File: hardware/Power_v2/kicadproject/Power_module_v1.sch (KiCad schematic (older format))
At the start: 63 parts, among them J1 Conn_01x02, J2 Conn_02x03_motherboardconn, J3 USB_B_Micro, J4 Conn_01x02_battery, J5 Conn_01x06_programmer, J6 Conn_01x06_programmer, SW1 SW_Push, U1 BQ24040, U2 BQ25570, U3 TPS705, U4 PIC16F18446

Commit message: Power: HW buck layout
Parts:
- added CBATT1, COUT3, CSTOR2: DNP, Capacitor_SMD:C_0805_2012Metric_Pad1.18x1.45mm_HandSolder, symbol Device:C
- added CIN2: 100n, Capacitor_SMD:C_0805_2012Metric_Pad1.18x1.45mm_HandSolder, symbol Device:C
- added COUT2: 22 uF, Capacitor_SMD:C_0805_2012Metric_Pad1.18x1.45mm_HandSolder, symbol Device:C
- C1, C10, C11, C12, C13, C14, C2, C3, C4, C7, C8, C9, CBYP1, CIN1, CREF1, CSTOR1: footprint Capacitor_SMD:C_0805_2012Metric_Pad1.15x1.40mm_HandSolder -> Capacitor_SMD:C_0805_2012Metric_Pad1.18x1.45mm_HandSolder
- COUT1: value 22 uF -> 100n; footprint Capacitor_SMD:C_0805_2012Metric_Pad1.15x1.40mm_HandSolder -> Capacitor_SMD:C_0805_2012Metric_Pad1.18x1.45mm_HandSolder
- J3: symbol Connector:USB_B_Micro -> Power_module_v1-rescue:USB_B_Micro-Connector
- S1, S2, S3: symbol TPS22860:TPS22860 -> Power_module_v1-rescue:TPS22860-TPS22860
- U1: symbol BQ24040:BQ24040 -> Power_module_v1-rescue:BQ24040-BQ24040
- U3: symbol tps7a05:TPS705 -> Power_module_v1-rescue:TPS705-tps7a05
- U4: symbol PIC16F18446SSOP20pin:PIC16F18446 -> Power_module_v1-rescue:PIC16F18446-PIC16F18446SSOP20pin
- renumbered C5 to COUT4, ROK3 to ROK1, ROK1 to ROK3, ROUT2 to ROUT1, ROUT1 to ROUT2, ROV2 to ROV1, ROV1 to ROV2
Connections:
- net 3V3BUCK: now also COUT2.1, COUT3.1
- net BAT+: now also CBATT1.1
- net GND: now also CBATT1.2, CIN2.2, COUT2.2, COUT3.2, CSTOR2.2
- net SOL+: now also CIN2.1
- net VSTOR: now also CSTOR2.1
- net nCHG: now reaches U4.5 (RC5)
- net nCHG: now also D2.1 (K), U1.8 (/CHG)
- no-connect marks 18 -> 17
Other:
- note added: "TODO\nCheck values"
- note added: "X7R\n"
- moved on the sheet: C10, C6, C7, CBYP1, COUT4, CSTOR1, D2, R5, S1

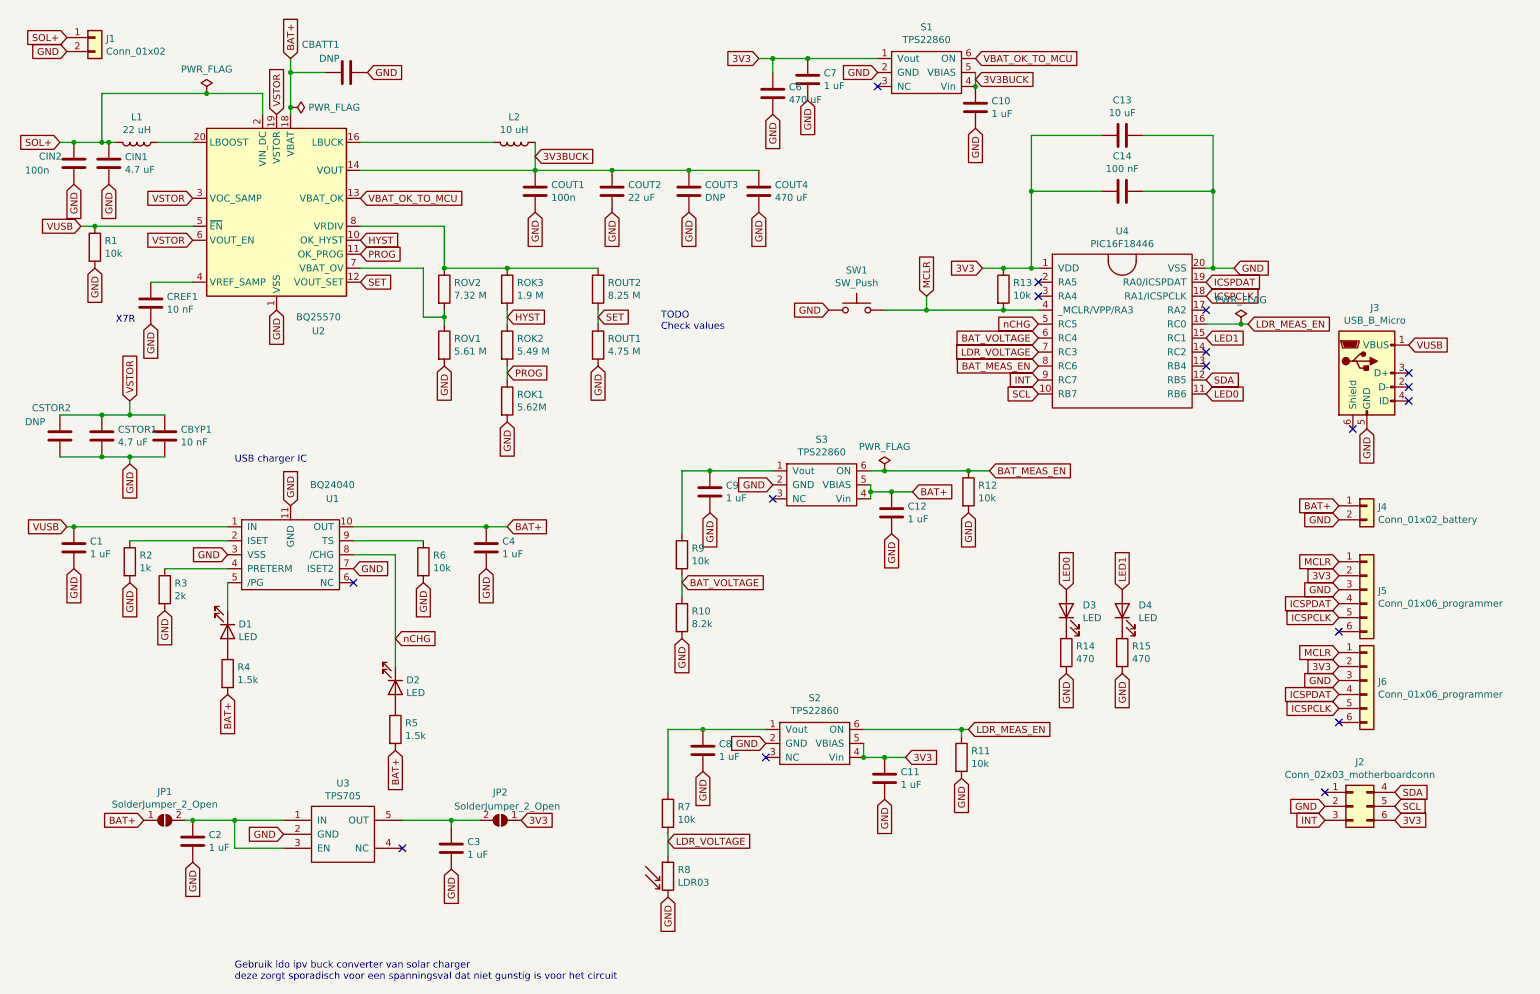
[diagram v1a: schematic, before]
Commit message: Power module HW redesign v2.0
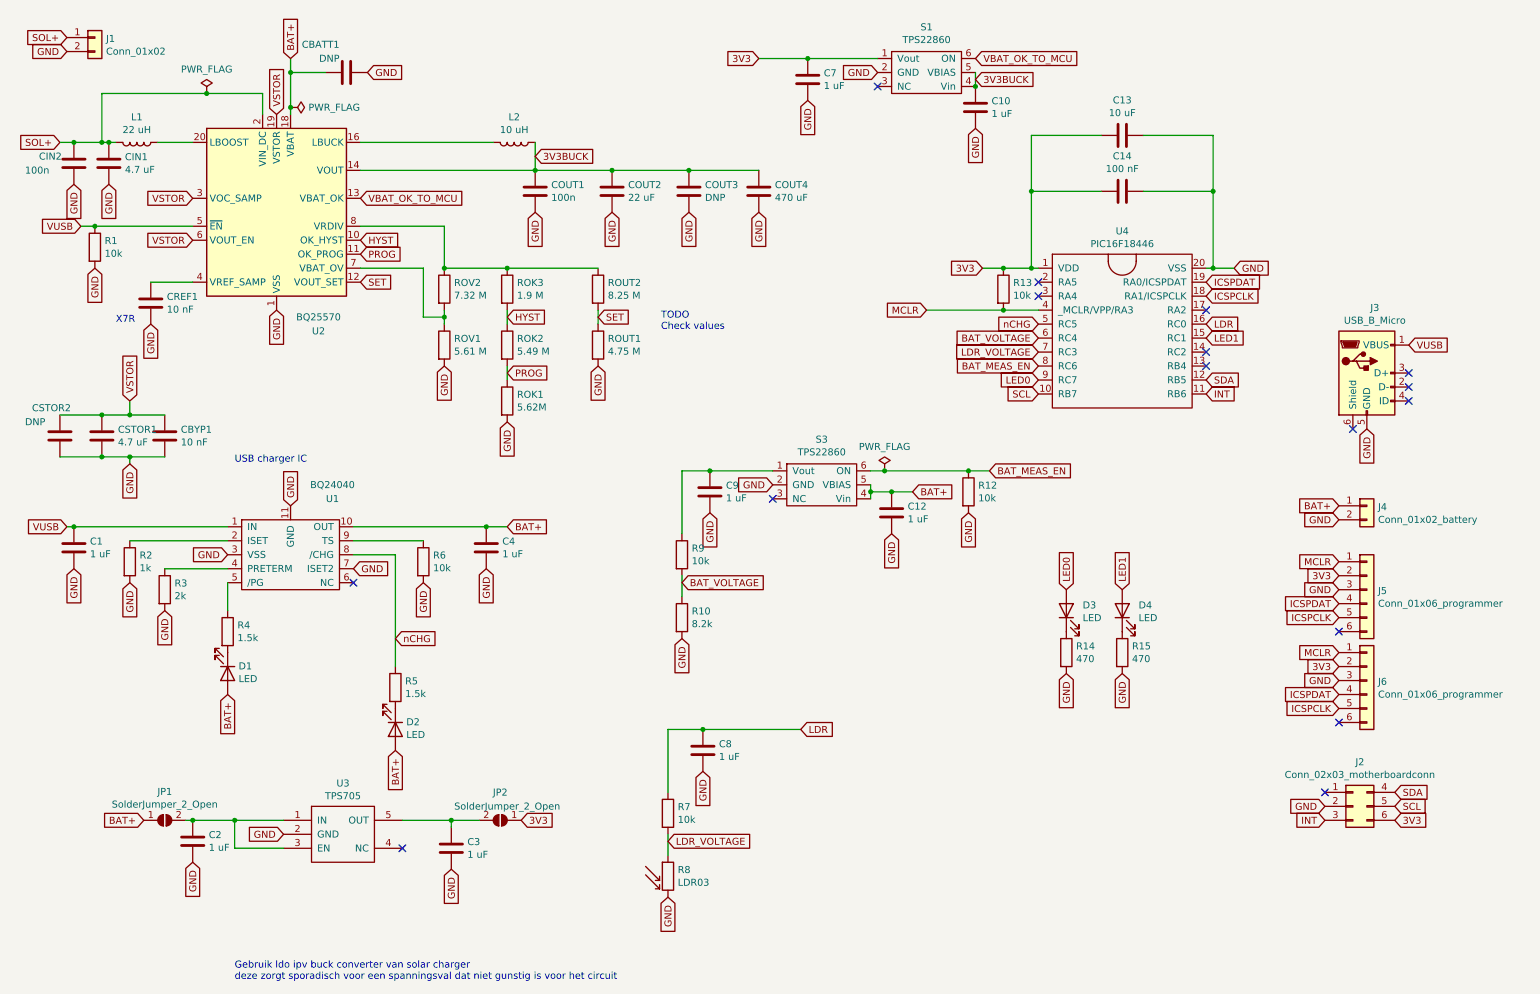
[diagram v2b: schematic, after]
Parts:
- removed C11: 1 uF, Capacitor_SMD:C_0805_2012Metric_Pad1.18x1.45mm_HandSolder, symbol Device:C
- removed C6: 470 uF, Capacitor_THT:CP_Radial_D6.3mm_P2.50mm, symbol Device:C
- removed R11: 10k, Resistor_SMD:R_0805_2012Metric_Pad1.15x1.40mm_HandSolder, symbol Device:R
- removed S2: TPS22860, Package_TO_SOT_SMD:SOT-23-6_Handsoldering, symbol Power_module_v1-rescue:TPS22860-TPS22860
- removed SW1: SW_Push, Button_Switch_THT:SW_PUSH_6mm_H7.3mm, symbol Switch:SW_Push
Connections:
- net LDR_MEAS_EN is gone; now on net LDR: U4.16 (RC0)
- net BAT+: now also D1.2 (A), D2.2 (A); no longer R4.2, R5.2
- net INT: now also U4.11 (RB6); no longer U4.9 (RC7)
- net LED0: now also U4.9 (RC7); no longer U4.11 (RB6)
- net nCHG: now also R5.1; no longer D2.1 (K)
- net at U1.5 (/PG): now also R4.1; no longer D1.1 (K)
- net LDR: now reaches C8.1, R7.1
- new net: D1.1 (K), R4.2
- new net: D2.1 (K), R5.2
- no-connect marks 17 -> 16
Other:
- moved on the sheet: D1, D2
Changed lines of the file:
@@
 L Device:LED D1
 U 1 1 5EE159F7
-P 1950 4900
-F 0 "D1" V 1897 4978 50  0000 L CNN
-F 1 "LED" V 1988 4978 50  0000 L CNN
-F 2 "LED_SMD:LED_0805_2012Metric_Pad1.15x1.40mm_HandSolder" H 1950 4900 50  0001 C CNN
-F 3 "~" H 1950 4900 50  0001 C CNN
-	1    1950 4900
-	0    1    1    0
-$EndComp
-Wire Wire Line
-	1950 4550 1950 4750
-$Comp
-L Device:R R4
-U 1 1 5EE1732A
 P 1950 5200
-F 0 "R4" H 2020 5246 50  0000 L CNN
-F 1 "1.5k" H 2020 5155 50  0000 L CNN
-F 2 "Resistor_SMD:R_0805_2012Metric_Pad1.15x1.40mm_HandSolder" V 1880 5200 50  0001 C CNN
+F 0 "D1" V 1897 5278 50  0000 L CNN
+F 1 "LED" V 1988 5278 50  0000 L CNN
+F 2 "LED_SMD:LED_0805_2012Metric_Pad1.15x1.40mm_HandSolder" H 1950 5200 50  0001 C CNN
 F 3 "~" H 1950 5200 50  0001 C CNN
 	1    1950 5200
-	1    0    0    -1
-$EndComp
+	0    1    1    0
+$EndComp
+Wire Wire Line
+	1950 4550 1950 4750
 Text GLabel 1950 5350 3    50   Input ~ 0
 BAT+
@@
 L Device:LED D2
 U 1 1 5EE1A8AA
-P 3150 5300
-F 0 "D2" V 3097 5378 50  0000 L CNN
-F 1 "LED" V 3188 5378 50  0000 L CNN
-F 2 "LED_SMD:LED_0805_2012Metric_Pad1.15x1.40mm_HandSolder" H 3150 5300 50  0001 C CNN
-F 3 "~" H 3150 5300 50  0001 C CNN
-	1    3150 5300
-	0    1    1    0
-$EndComp
-$Comp
-L Device:R R5
-U 1 1 5EE1A8B0
 P 3150 5600
-F 0 "R5" H 3220 5646 50  0000 L CNN
-F 1 "1.5k" H 3220 5555 50  0000 L CNN
-F 2 "Resistor_SMD:R_0805_2012Metric_Pad1.15x1.40mm_HandSolder" V 3080 5600 50  0001 C CNN
+F 0 "D2" V 3097 5678 50  0000 L CNN
+F 1 "LED" V 3188 5678 50  0000 L CNN
+F 2 "LED_SMD:LED_0805_2012Metric_Pad1.15x1.40mm_HandSolder" H 3150 5600 50  0001 C CNN
 F 3 "~" H 3150 5600 50  0001 C CNN
 	1    3150 5600
-	1    0    0    -1
+	0    1    1    0
 $EndComp
 Text GLabel 3150 5750 3    50   Input ~ 0
@@
 Text GLabel 7950 4600 1    50   Input ~ 0
 LED0
-Text GLabel 8950 3200 2    50   Input ~ 0
-LED0
-Text GLabel 6800 5800 2    50   Input ~ 0
-3V3
 Text GLabel 8350 4600 1    50   Input ~ 0
 LED1
@@
 	1    0    0    -1
 $EndComp
-$Comp
-L Power_module_v1-rescue:TPS22860-TPS22860 S2
-U 1 1 5EE4AA8C
-P 5900 5850
-F 0 "S2" H 6150 6325 50  0000 C CNN
-F 1 "TPS22860" H 6150 6234 50  0000 C CNN
-F 2 "Package_TO_SOT_SMD:SOT-23-6_Handsoldering" H 5900 5850 50  0001 C CNN
-F 3 "" H 5900 5850 50  0001 C CNN
-	1    5900 5850
-	1    0    0    -1
-$EndComp
-NoConn ~ 5800 5800
 NoConn ~ 5850 3950
 Text GLabel 6850 3900 2    50   Input ~ 0
@@
 Text GLabel 7750 2900 0    50   Input ~ 0
 LDR_VOLTAGE
-Text GLabel 9250 2700 2    50   Input ~ 0
-LDR_MEAS_EN
-Text GLabel 7250 5600 2    50   Input ~ 0
-LDR_MEAS_EN
-Wire Wire Line
-	6500 5800 6650 5800
-$Comp
-L Device:C C11
-U 1 1 5EE5C853
-P 6650 5950
-F 0 "C11" H 6765 5996 50  0000 L CNN
-F 1 "1 uF" H 6765 5905 50  0000 L CNN
-F 2 "Capacitor_SMD:C_0805_2012Metric_Pad1.18x1.45mm_HandSolder" H 6688 5800 50  0001 C CNN
-F 3 "~" H 6650 5950 50  0001 C CNN
-	1    6650 5950
-	1    0    0    -1
-$EndComp
-Connection ~ 6650 5800
-Wire Wire Line
-	6650 5800 6800 5800
-Text GLabel 6650 6100 3    50   Input ~ 0
-GND
-Wire Wire Line
-	6500 5700 6500 5800
-Connection ~ 6500 5800
-Text GLabel 5800 5700 0    50   Input ~ 0
-GND
 Text GLabel 8950 2400 2    50   Input ~ 0
 ICSPDAT
 Text GLabel 8950 2500 2    50   Input ~ 0
 ICSPCLK
-Text GLabel 6950 2500 1    50   Input ~ 0
-MCLR
 Wire Wire Line
 	7750 2600 7500 2600
@@
 Text GLabel 7750 3200 0    50   Input ~ 0
 SCL
-Text GLabel 7750 3100 0    50   Input ~ 0
+Text GLabel 8950 3200 2    50   Input ~ 0
 INT
-Wire Wire Line
-	9200 2700 8950 2700
-Wire Wire Line
-	9200 2700 9250 2700
-Connection ~ 9200 2700
-$Comp
-L power:PWR_FLAG #FLG04
-U 1 1 5EE9D631
-P 9200 2700
-F 0 "#FLG04" H 9200 2775 50  0001 C CNN
-F 1 "PWR_FLAG" H 9200 2873 50  0000 C CNN
-F 2 "" H 9200 2700 50  0001 C CNN
-F 3 "~" H 9200 2700 50  0001 C CNN
-	1    9200 2700
-	1    0    0    -1
-$EndComp
 $Comp
 L Power_module_v1-rescue:TPS705-tps7a05 U3
@@
 Text GLabel 5750 1900 3    50   Input ~ 0
 GND
-$Comp
-L Device:C C6
-U 1 1 5F36379B
-P 5850 1050
-F 0 "C6" H 5965 1096 50  0000 L CNN
-F 1 "470 uF" H 5965 1005 50  0000 L CNN
-F 2 "Capacitor_THT:CP_Radial_D6.3mm_P2.50mm" H 5888 900 50  0001 C CNN
-F 3 "~" H 5850 1050 50  0001 C CNN
-	1    5850 1050
-	1    0    0    -1
-$EndComp
-Text GLabel 5850 1200 3    50   Input ~ 0
-GND
-Wire Wire Line
-	5750 800  5850 800
-Wire Wire Line
-	5850 900  5850 800
-Connection ~ 5850 800
 Wire Wire Line
 	6650 3750 7250 3750
@@
 Text GLabel 7250 4050 3    50   Input ~ 0
 GND
-$Comp
-L Device:R R11
-U 1 1 5F372BE5
-P 7200 5800
-F 0 "R11" H 7270 5846 50  0000 L CNN
-F 1 "10k" H 7270 5755 50  0000 L CNN
-F 2 "Resistor_SMD:R_0805_2012Metric_Pad1.15x1.40mm_HandSolder" V 7130 5800 50  0001 C CNN
-F 3 "~" H 7200 5800 50  0001 C CNN
-	1    7200 5800
-	1    0    0    -1
-$EndComp
-Text GLabel 7200 5950 3    50   Input ~ 0
-GND
-Wire Wire Line
-	7250 5600 7200 5600
-Wire Wire Line
-	7200 5650 7200 5600
-Connection ~ 7200 5600
-Wire Wire Line
-	7200 5600 6500 5600
 Wire Wire Line
 	5200 3750 5400 3750
@@
 Text GLabel 6100 1100 3    50   Input ~ 0
 GND
-Wire Wire Line
-	5850 800  6100 800
 Connection ~ 6100 800
 Wire Wire Line
 	6100 800  6600 800
-Connection ~ 5350 5600
-Wire Wire Line
-	5350 5600 5800 5600
 Connection ~ 5400 3750
 Wire Wire Line
 	5400 3750 5850 3750
 NoConn ~ 9800 6050
-$Comp
-L Switch:SW_Push SW1
-U 1 1 5F430BA9
-P 6450 2600
-F 0 "SW1" H 6450 2885 50  0000 C CNN
-F 1 "SW_Push" H 6450 2794 50  0000 C CNN
-F 2 "Button_Switch_THT:SW_PUSH_6mm_H7.3mm" H 6450 2800 50  0001 C CNN
-F 3 "~" H 6450 2800 50  0001 C CNN
-	1    6450 2600
-	1    0    0    -1
-$EndComp
-Text GLabel 6250 2600 0    50   Input ~ 0
-GND
-Wire Wire Line
-	6650 2600 6950 2600
-Wire Wire Line
-	6950 2500 6950 2600
-Connection ~ 6950 2600
-Wire Wire Line
-	6950 2600 7500 2600
 $Comp
 L Sensor_Optical:LDR03 R8
@@
 Text Notes 5050 2750 0    50   ~ 0
 TODO\nCheck values
+Wire Wire Line
+	6950 2600 7500 2600
+Text GLabel 6950 2600 0    50   Input ~ 0
+MCLR
+$Comp
+L Device:R R5
+U 1 1 5FC84F8B
+P 3150 5300
+F 0 "R5" H 3220 5346 50  0000 L CNN
+F 1 "1.5k" H 3220 5255 50  0000 L CNN
+F 2 "Resistor_SMD:R_0805_2012Metric_Pad1.15x1.40mm_HandSolder" V 3080 5300 50  0001 C CNN
+F 3 "~" H 3150 5300 50  0001 C CNN
+	1    3150 5300
+	1    0    0    -1
+$EndComp
+$Comp
+L Device:R R4
+U 1 1 5FC94B37
+P 1950 4900
+F 0 "R4" H 2020 4946 50  0000 L CNN
+F 1 "1.5k" H 2020 4855 50  0000 L CNN
+F 2 "Resistor_SMD:R_0805_2012Metric_Pad1.15x1.40mm_HandSolder" V 1880 4900 50  0001 C CNN
+F 3 "~" H 1950 4900 50  0001 C CNN
+	1    1950 4900
+	1    0    0    -1
+$EndComp
+Wire Wire Line
+	5750 800  6100 800
+Wire Wire Line
+	5350 5600 6050 5600
+Connection ~ 5350 5600
+Text GLabel 8950 2700 2    50   Input ~ 0
+LDR
+Text GLabel 6050 5600 2    50   Input ~ 0
+LDR
+Text GLabel 7750 3100 0    50   Input ~ 0
+LED0
 $EndSCHEMATC

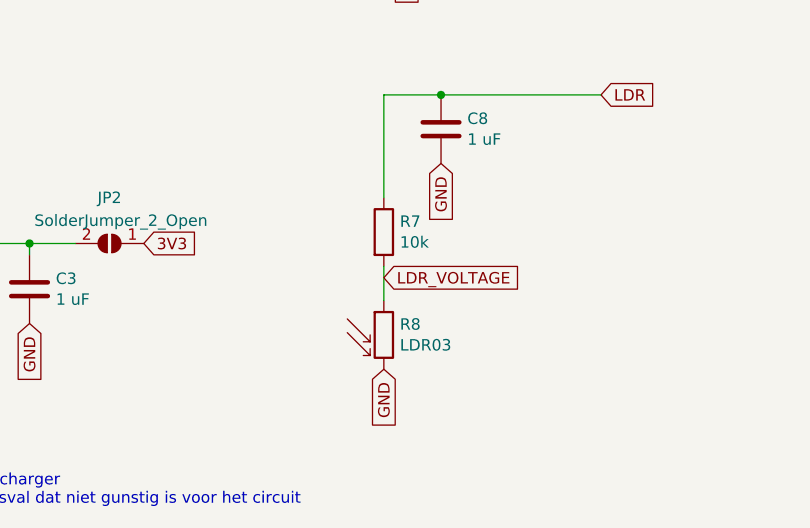
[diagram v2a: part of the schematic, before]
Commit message: Power HW: fixed LDR voltage divider
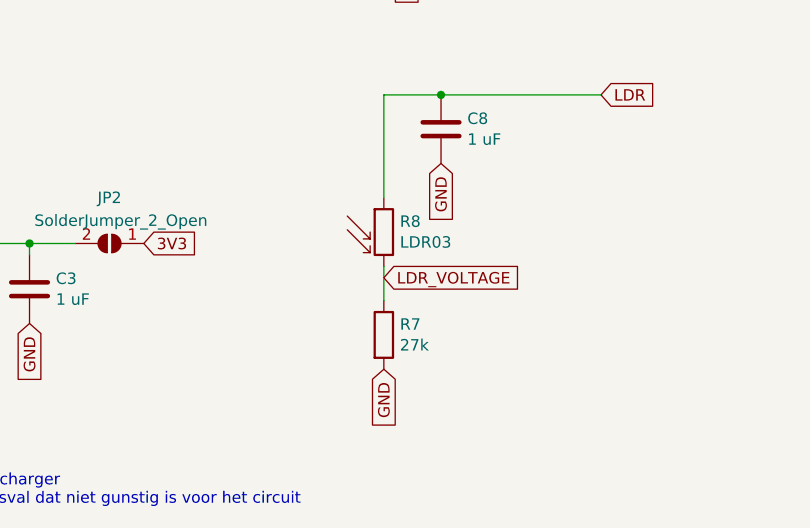
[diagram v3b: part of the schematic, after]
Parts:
- R7: value 10k -> 27k
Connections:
- net GND: now also R7.2; no longer R8.2
- net LDR: now also R8.1; no longer R7.1
- net LDR_VOLTAGE: now also R7.1, R8.2; no longer R7.2, R8.1
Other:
- moved on the sheet: R7, R8
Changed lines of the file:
@@
 L Device:R R7
 U 1 1 5EE5A834
-P 5100 6200
-F 0 "R7" H 5170 6246 50  0000 L CNN
-F 1 "10k" H 5170 6155 50  0000 L CNN
-F 2 "Resistor_SMD:R_0805_2012Metric_Pad1.15x1.40mm_HandSolder" V 5030 6200 50  0001 C CNN
-F 3 "~" H 5100 6200 50  0001 C CNN
-	1    5100 6200
+P 5100 6650
+F 0 "R7" H 5170 6696 50  0000 L CNN
+F 1 "27k" H 5170 6605 50  0000 L CNN
+F 2 "Resistor_SMD:R_0805_2012Metric_Pad1.15x1.40mm_HandSolder" V 5030 6650 50  0001 C CNN
+F 3 "~" H 5100 6650 50  0001 C CNN
+	1    5100 6650
 	1    0    0    -1
 $EndComp
@@
 L Sensor_Optical:LDR03 R8
 U 1 1 5F3A3DD1
-P 5100 6650
-F 0 "R8" H 5170 6696 50  0000 L CNN
-F 1 "LDR03" H 5170 6605 50  0000 L CNN
-F 2 "OptoDevice:R_LDR_5.1x4.3mm_P3.4mm_Vertical" V 5275 6650 50  0001 C CNN
-F 3 "http://www.elektronica-componenten.nl/WebRoot/StoreNL/Shops/61422969/54F1/BA0C/C664/31B9/2173/C0A8/2AB9/2AEF/LDR03IMP.pdf" H 5100 6600 50  0001 C CNN
-	1    5100 6650
-	1    0    0    -1
-$EndComp
+P 5100 6200
+F 0 "R8" H 5170 6246 50  0000 L CNN
+F 1 "LDR03" H 5170 6155 50  0000 L CNN
+F 2 "OptoDevice:R_LDR_5.1x4.3mm_P3.4mm_Vertical" V 5275 6200 50  0001 C CNN
+F 3 "http://www.elektronica-componenten.nl/WebRoot/StoreNL/Shops/61422969/54F1/BA0C/C664/31B9/2173/C0A8/2AB9/2AEF/LDR03IMP.pdf" H 5100 6150 50  0001 C CNN
+	1    5100 6200
+	1    0    0    -1
+$EndComp
